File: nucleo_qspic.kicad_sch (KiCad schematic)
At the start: 12 parts, among them IC1 W25Q32JVSFIQ, U1 NUCLEO144-H743ZI

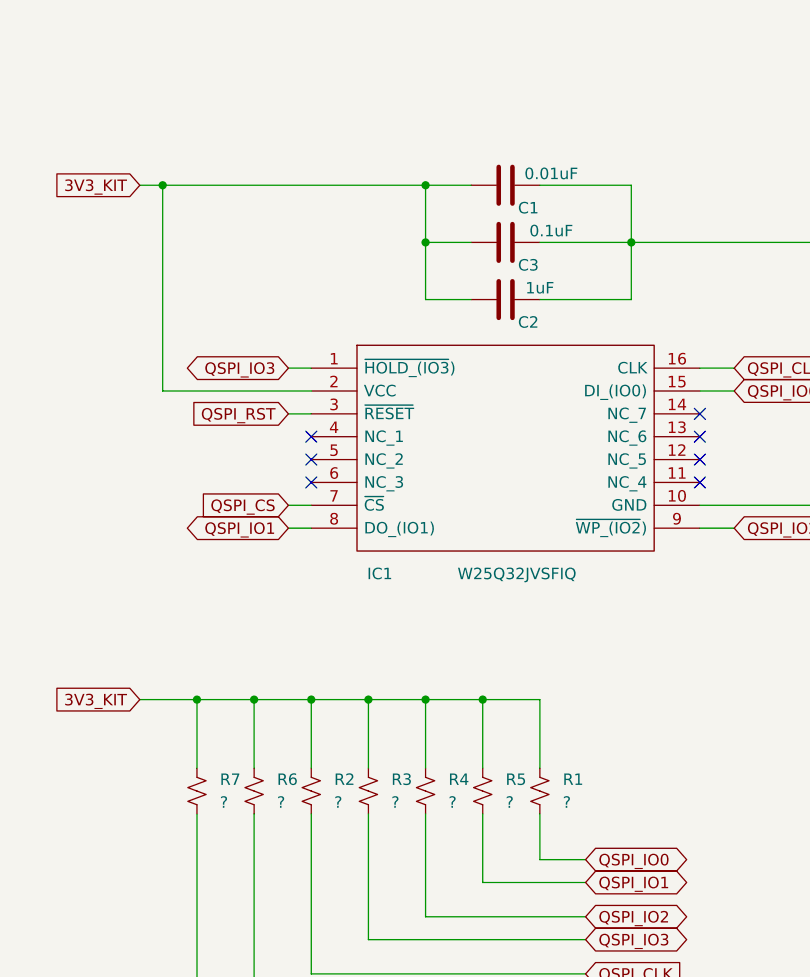
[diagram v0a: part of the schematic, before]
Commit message: make clk line width same with other qspi signal, give pull up value to 10K(optional) and change capacitance value to what is available in inventory
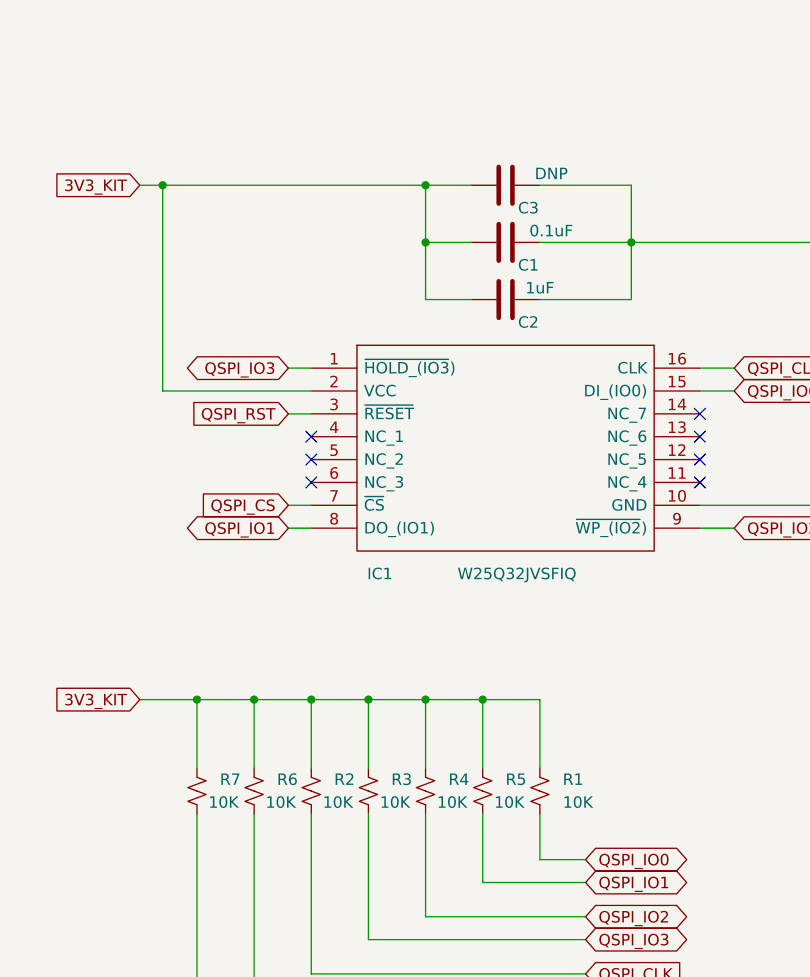
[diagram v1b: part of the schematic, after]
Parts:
- C3: renamed from C1; value 0.01uF -> DNP
- R1, R2, R3, R4, R5, R6, R7: value ? -> 10K
- U1: footprint (none) -> custom_nucleo_144:ST_Morpho_Connector_144_STLink_MountingHoles
- renumbered C3 to C1
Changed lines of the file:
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@@
       (effects (font (size 1.27 1.27)) (justify left))
     )
-    (property "Value" "?" (id 1) (at 303.53 152.3999 0)
+    (property "Value" "10K" (id 1) (at 303.53 152.3999 0)
       (effects (font (size 1.27 1.27)) (justify left))
     )
@@
   )
   (symbol (lib_id "Device:R_Small_US") (at 281.94 151.13 0) (unit 1)
-    (in_bom yes) (on_board yes) (fields_autoplaced)
+    (in_bom yes) (on_board yes)
     (property "Reference" "R3" (id 0) (at 284.48 149.8599 0)
       (effects (font (size 1.27 1.27)) (justify left))
     )
-    (property "Value" "?" (id 1) (at 284.48 152.3999 0)
+    (property "Value" "10K" (id 1) (at 283.21 152.4 0)
       (effects (font (size 1.27 1.27)) (justify left))
     )
@@
   )
   (symbol (lib_id "Device:R_Small_US") (at 275.59 151.13 0) (unit 1)
-    (in_bom yes) (on_board yes) (fields_autoplaced)
+    (in_bom yes) (on_board yes)
     (property "Reference" "R2" (id 0) (at 278.13 149.8599 0)
       (effects (font (size 1.27 1.27)) (justify left))
     )
-    (property "Value" "?" (id 1) (at 278.13 152.3999 0)
+    (property "Value" "10K" (id 1) (at 276.86 152.4 0)
       (effects (font (size 1.27 1.27)) (justify left))
     )
@@
   (symbol (lib_id "Device:C") (at 297.18 90.17 270) (unit 1)
     (in_bom yes) (on_board yes)
-    (property "Reference" "C3" (id 0) (at 299.72 92.71 90))
+    (property "Reference" "C1" (id 0) (at 299.72 92.71 90))
     (property "Value" "0.1uF" (id 1) (at 302.26 88.9 90))
     (property "Footprint" "Capacitor_SMD:C_0805_2012Metric" (id 2) (at 293.37 91.1352 0)
@@
   )
   (symbol (lib_id "Device:R_Small_US") (at 269.24 151.13 0) (unit 1)
-    (in_bom yes) (on_board yes) (fields_autoplaced)
+    (in_bom yes) (on_board yes)
     (property "Reference" "R6" (id 0) (at 271.78 149.8599 0)
       (effects (font (size 1.27 1.27)) (justify left))
     )
-    (property "Value" "?" (id 1) (at 271.78 152.3999 0)
+    (property "Value" "10K" (id 1) (at 270.51 152.4 0)
       (effects (font (size 1.27 1.27)) (justify left))
     )
@@
   (symbol (lib_id "Device:C") (at 297.18 83.82 270) (unit 1)
     (in_bom yes) (on_board yes)
-    (property "Reference" "C1" (id 0) (at 299.72 86.36 90))
-    (property "Value" "0.01uF" (id 1) (at 302.26 82.55 90))
+    (property "Reference" "C3" (id 0) (at 299.72 86.36 90))
+    (property "Value" "DNP" (id 1) (at 302.26 82.55 90))
     (property "Footprint" "Capacitor_SMD:C_0805_2012Metric" (id 2) (at 293.37 84.7852 0)
       (effects (font (size 1.27 1.27)) hide)
@@
       (effects (font (size 1.27 1.27)) (justify left))
     )
-    (property "Footprint" "" (id 2) (at 171.45 232.41 0)
+    (property "Footprint" "custom_nucleo_144:ST_Morpho_Connector_144_STLink_MountingHoles" (id 2) (at 171.45 232.41 0)
       (effects (font (size 1.27 1.27)) (justify left) hide)
     )
@@
   )
   (symbol (lib_id "Device:R_Small_US") (at 262.89 151.13 0) (unit 1)
-    (in_bom yes) (on_board yes) (fields_autoplaced)
+    (in_bom yes) (on_board yes)
     (property "Reference" "R7" (id 0) (at 265.43 149.8599 0)
       (effects (font (size 1.27 1.27)) (justify left))
     )
-    (property "Value" "?" (id 1) (at 265.43 152.3999 0)
+    (property "Value" "10K" (id 1) (at 264.16 152.4 0)
       (effects (font (size 1.27 1.27)) (justify left))
     )
@@
   )
   (symbol (lib_id "Device:R_Small_US") (at 288.29 151.13 0) (unit 1)
-    (in_bom yes) (on_board yes) (fields_autoplaced)
+    (in_bom yes) (on_board yes)
     (property "Reference" "R4" (id 0) (at 290.83 149.8599 0)
       (effects (font (size 1.27 1.27)) (justify left))
     )
-    (property "Value" "?" (id 1) (at 290.83 152.3999 0)
+    (property "Value" "10K" (id 1) (at 289.56 152.4 0)
       (effects (font (size 1.27 1.27)) (justify left))
     )
@@
   )
   (symbol (lib_id "Device:R_Small_US") (at 294.64 151.13 0) (unit 1)
-    (in_bom yes) (on_board yes) (fields_autoplaced)
+    (in_bom yes) (on_board yes)
     (property "Reference" "R5" (id 0) (at 297.18 149.8599 0)
       (effects (font (size 1.27 1.27)) (justify left))
     )
-    (property "Value" "?" (id 1) (at 297.18 152.3999 0)
+    (property "Value" "10K" (id 1) (at 295.91 152.4 0)
       (effects (font (size 1.27 1.27)) (justify left))
     )
@@
       (reference "#PWR02") (unit 1) (value "GNDD") (footprint "")
     )
-    (path "/7b91c446-d55e-414c-8600-6e86cc6eeb30"
-      (reference "C1") (unit 1) (value "0.01uF") (footprint "Capacitor_SMD:C_0805_2012Metric")
+    (path "/7465597a-e4a0-4b89-86dd-a4e9c3c50249"
+      (reference "C1") (unit 1) (value "0.1uF") (footprint "Capacitor_SMD:C_0805_2012Metric")
     )
     (path "/32d29073-647d-4ccf-9ad2-bab625bf6190"
       (reference "C2") (unit 1) (value "1uF") (footprint "Capacitor_SMD:C_0805_2012Metric")
     )
-    (path "/7465597a-e4a0-4b89-86dd-a4e9c3c50249"
-      (reference "C3") (unit 1) (value "0.1uF") (footprint "Capacitor_SMD:C_0805_2012Metric")
+    (path "/7b91c446-d55e-414c-8600-6e86cc6eeb30"
+      (reference "C3") (unit 1) (value "DNP") (footprint "Capacitor_SMD:C_0805_2012Metric")
     )
     (path "/266c7456-0eed-4e89-aa25-9d5223777258"
@@
     )
     (path "/455b218f-5e4f-4d55-8ee3-7f484b2a4a5c"
-      (reference "R1") (unit 1) (value "?") (footprint "Resistor_SMD:R_0805_2012Metric")
+      (reference "R1") (unit 1) (value "10K") (footprint "Resistor_SMD:R_0805_2012Metric")
     )
     (path "/592448e3-a2ee-41a5-9d0c-606155fb65ee"
-      (reference "R2") (unit 1) (value "?") (footprint "Resistor_SMD:R_0805_2012Metric")
+      (reference "R2") (unit 1) (value "10K") (footprint "Resistor_SMD:R_0805_2012Metric")
     )
     (path "/54d18d59-3d8b-4308-9f78-fbe691e703a6"
-      (reference "R3") (unit 1) (value "?") (footprint "Resistor_SMD:R_0805_2012Metric")
+      (reference "R3") (unit 1) (value "10K") (footprint "Resistor_SMD:R_0805_2012Metric")
     )
     (path "/8ddc0adc-6df3-484d-802e-a75ed4f98638"
-      (reference "R4") (unit 1) (value "?") (footprint "Resistor_SMD:R_0805_2012Metric")
+      (reference "R4") (unit 1) (value "10K") (footprint "Resistor_SMD:R_0805_2012Metric")
     )
     (path "/aa838d7e-ef4a-4c6d-b14b-48deee7c8790"
-      (reference "R5") (unit 1) (value "?") (footprint "Resistor_SMD:R_0805_2012Metric")
+      (reference "R5") (unit 1) (value "10K") (footprint "Resistor_SMD:R_0805_2012Metric")
     )
     (path "/79729647-0731-4485-a8e7-99a5fbf14649"
-      (reference "R6") (unit 1) (value "?") (footprint "Resistor_SMD:R_0805_2012Metric")
+      (reference "R6") (unit 1) (value "10K") (footprint "Resistor_SMD:R_0805_2012Metric")
     )
     (path "/845b0a8a-33c6-430c-82d6-5308bb9cb32a"
-      (reference "R7") (unit 1) (value "?") (footprint "Resistor_SMD:R_0805_2012Metric")
+      (reference "R7") (unit 1) (value "10K") (footprint "Resistor_SMD:R_0805_2012Metric")
     )
     (path "/80974d09-14d4-49e4-885a-2070ecdadbdc"
